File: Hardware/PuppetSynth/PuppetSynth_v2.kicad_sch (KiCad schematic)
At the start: 37 parts, among them J1 ADS1115, J2 ADS1115, SW1 SW_Rotary_1x4_MP, SW2 SW_Rotary_1x4_MP, SW3 SW_Rotary_1x4_MP, SW4 SW_SP3T_NR01103, SW5 SW_SP3T_NR01103, SW6 SW_SP3T_NR01103, SW7 Switch

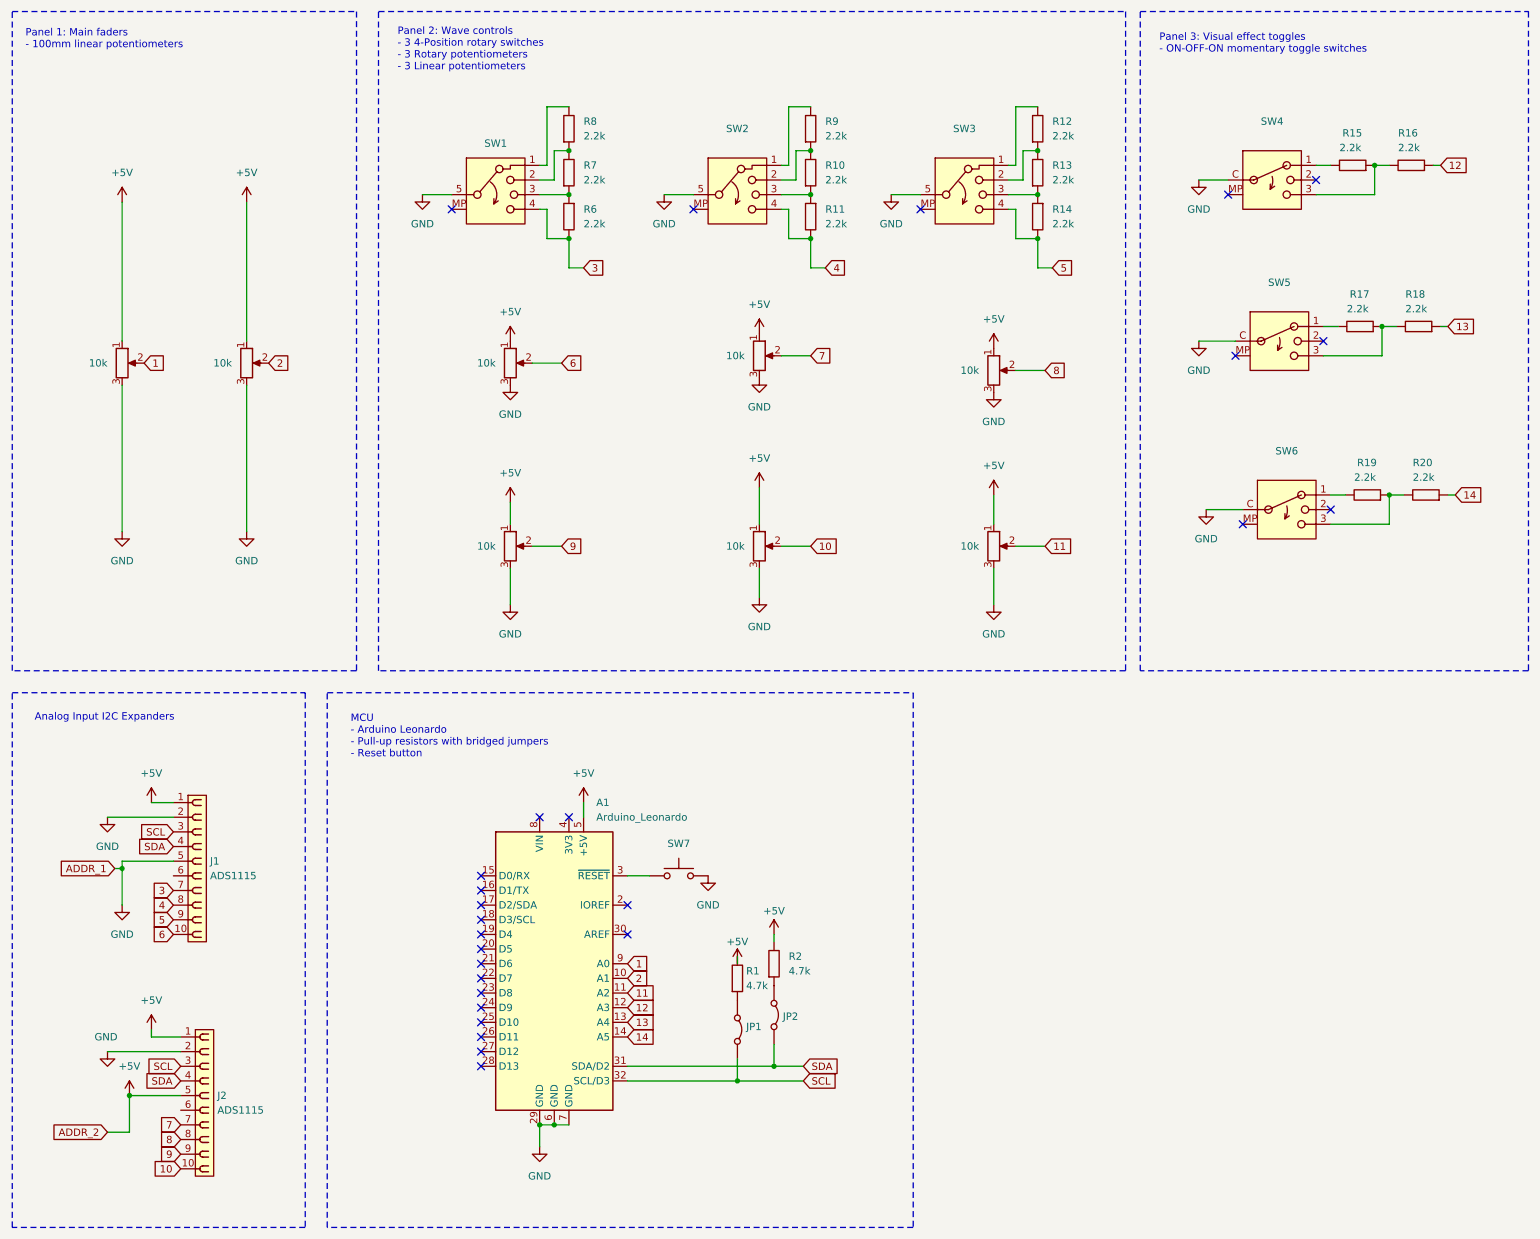
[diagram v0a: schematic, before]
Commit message: Updated code for prototype v2 and updated schematic
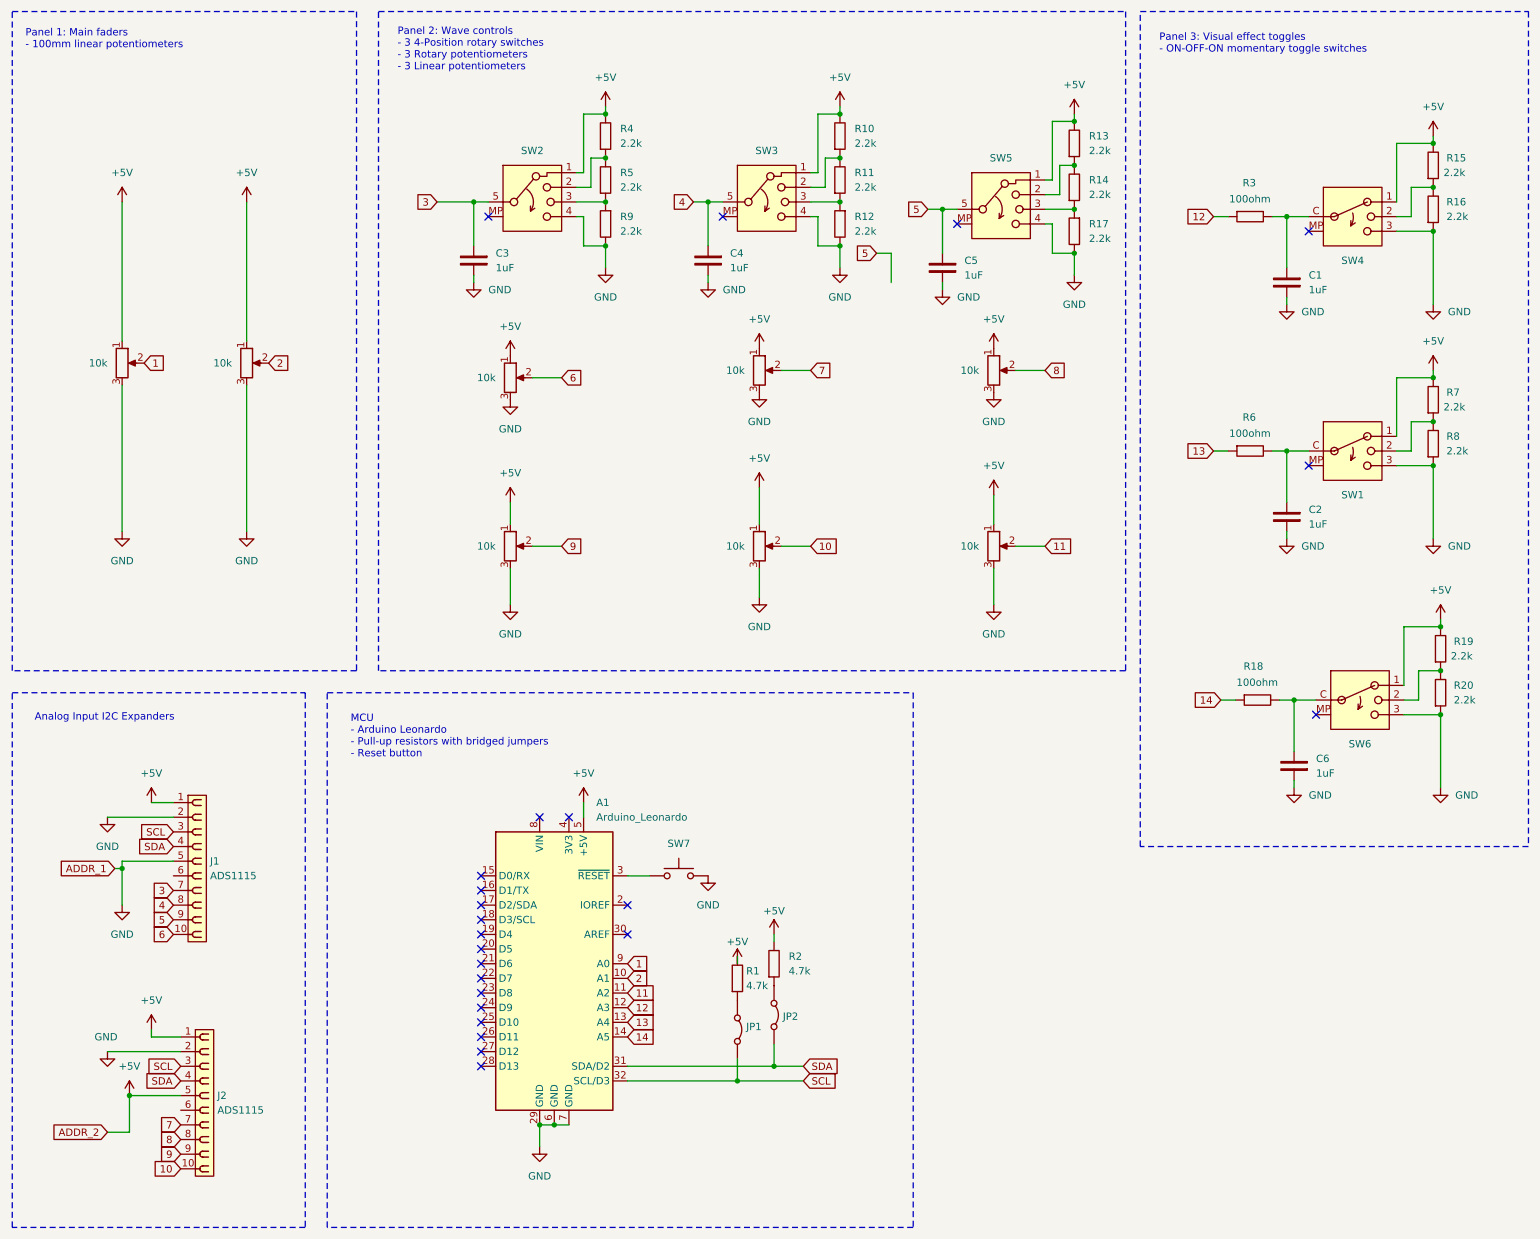
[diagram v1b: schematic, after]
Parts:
- removed SW1: SW_Rotary_1x4_MP, symbol Switch:SW_Rotary_1x4_MP
- removed SW5: SW_SP3T_NR01103, Button_Switch_THT:SW_NKK_NR01, symbol Switch:SW_SP3T_NR01103
- added C1, C2, C3, C4, C5, C6: 1uF, Capacitor_THT:C_Disc_D3.0mm_W2.0mm_P2.50mm, symbol PCM_SL_Devices:Capacitor_NP
- added R3: 100ohm, Resistor_THT:R_Axial_DIN0207_L6.3mm_D2.5mm_P10.16mm_Horizontal, symbol PCM_SL_Resistors:2.2k
- added R4, R5: 2.2k, Resistor_THT:R_Axial_DIN0207_L6.3mm_D2.5mm_P10.16mm_Horizontal, symbol PCM_SL_Resistors:2.2k
- added SW1: SW_SP3T_NR01103, Button_Switch_THT:SW_NKK_NR01, symbol Switch:SW_SP3T_NR01103
- added SW5: SW_Rotary_1x4_MP, symbol Switch:SW_Rotary_1x4_MP
- R18, R6: value 2.2k -> 100ohm
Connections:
- net +5V: now also R10.2, R13.2, R15.2, R19.2, R7.2, SW2.1, SW3.1, SW4.1, SW6.1, R4.2, SW1.1, SW5.1
- net 12: now also R3.1; no longer R16.1
- net 13: now also R6.1; no longer R18.1
- net 14: now also R18.1; no longer R20.1
- net 3: now also SW2.5, C3.1; no longer R6.2
- net 4: now also SW3.5, C4.1; no longer R11.2, SW2.4
- net 5: now also C5.1, SW5.5; no longer R14.2, SW3.4
- net GND: now also R12.2, R16.1, R17.2, R20.1, R8.1, R9.2, SW2.4, SW3.4, SW4.3, SW6.3, C1.2, C2.2, C3.2, C4.2, C5.2, C6.2, SW1.3, SW5.4; no longer SW2.5, SW3.5, SW4.C (Common), SW6.C (Common)
- net at R15.1, R16.2: now also SW4.2; no longer SW4.3
- net at R19.1, R20.2: now also SW6.2; no longer SW6.3
- net at R18.2: now also SW6.C (Common), C6.1; no longer R17.1
- net at R8.2: now also R7.1, SW1.2
- new net: R10.1, R11.2, SW3.2
- new net: R4.1, R5.2, SW2.2
- new net: R14.1, R17.1, SW5.3
- new net: R13.1, R14.2, SW5.2
- new net: R5.1, R9.1, SW2.3
- new net: C2.1, R6.2, SW1.C (Common)
- new net: R11.1, R12.1, SW3.3
- new net: C1.1, R3.2, SW4.C (Common)
- no-connect marks 27 -> 24
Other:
- title: "Puppet Synthesizer" -> "Puppet Synth"
- moved on the sheet: 10k, R15, R16, SW4
